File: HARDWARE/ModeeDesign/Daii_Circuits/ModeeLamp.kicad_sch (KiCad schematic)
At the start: 9 parts, among them J4 AC, J5 AC, Q5 2N2222, Q6 IRLZ44N, U5 MOC3023M, U6 ESP32-DEVKIT-V1

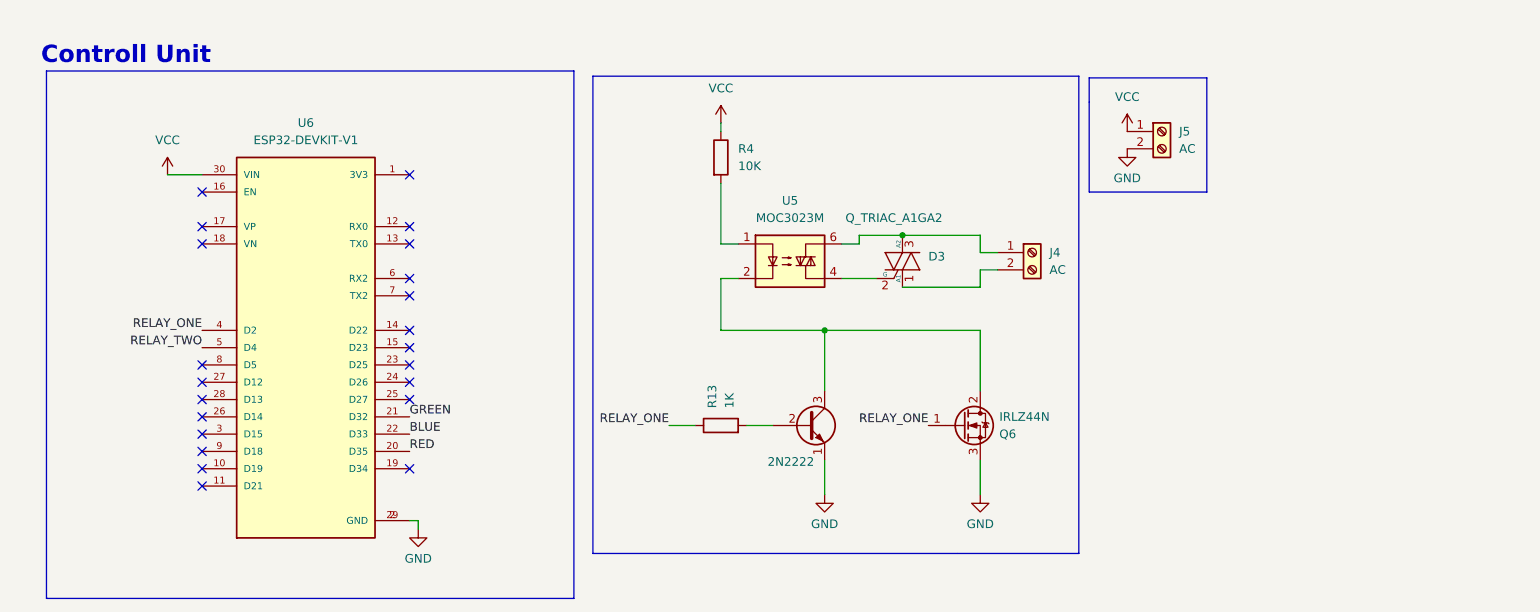
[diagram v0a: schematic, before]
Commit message: WIP: ModeeLamp PCB placement, heater project, Nakheel_Driver updates; ignore .history
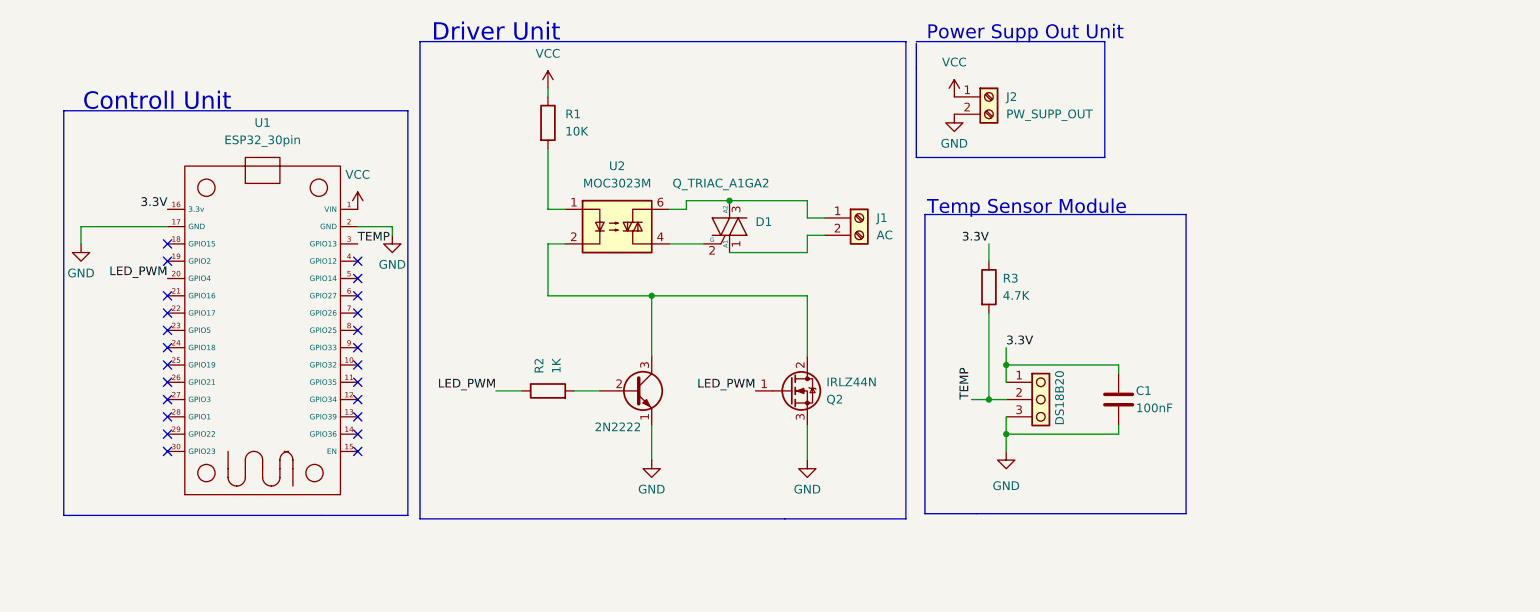
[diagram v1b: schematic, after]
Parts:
- removed U6: ESP32-DEVKIT-V1, RF:MODULE_ESP32_DEVKIT_V1, symbol ESP32-DEVKIT-V1:ESP32-DEVKIT-V1
- added C1: 100nF, Capacitor_THT:C_Disc_D5.0mm_W2.5mm_P2.50mm, symbol Device:C
- added J3: DS18B20, TerminalBlock_Altech:Altech_AK100_1x03_P5.00mm, symbol Connector:Screw_Terminal_01x03
- added R3: 4.7K, Resistor_THT:R_Axial_DIN0204_L3.6mm_D1.6mm_P7.62mm_Horizontal, symbol Device:R
- added U1: (no value), ESP32_30pin, symbol esp32_30pin_revised:ESP32_30Pin
- J1: renamed from J4; footprint TerminalBlock:TerminalBlock_Altech_AK300-2_P5.00mm -> TerminalBlock_Altech:Altech_AK100_1x02_P5.00mm
- J2: renamed from J5; value AC -> PW_SUPP_OUT; footprint TerminalBlock:TerminalBlock_Altech_AK300-2_P5.00mm -> TerminalBlock_Altech:Altech_AK100_1x02_P5.00mm
- renumbered D3 to D1, Q5 to Q1, Q6 to Q2, R4 to R1, R13 to R2, U5 to U2
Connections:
- net GND: now also C1.2, J3.3 (Pin_3), U1.17 (GND), U1.2 (GND)
- net VCC: now also U1.1 (VIN)
- net RELAY_ONE renamed LED_PWM
- net LED_PWM: now also U1.20 (GPIO4)
- new net 3.3V: C1.1, J3.1 (Pin_1), R3.1, U1.16 (3.3v)
- new net TEMP: J3.2 (Pin_2), R3.2, U1.3 (GPIO13)
- no-connect marks 22 -> 24
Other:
- note added: "Driver Unit"
- note added: "Power Supp Out Unit"
- note added: "Temp Sensor Module"
- moved on the sheet: D1, J1, J2, Q2, R1, R2, U2

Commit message: Fixing PCB review points and add interactive BOM
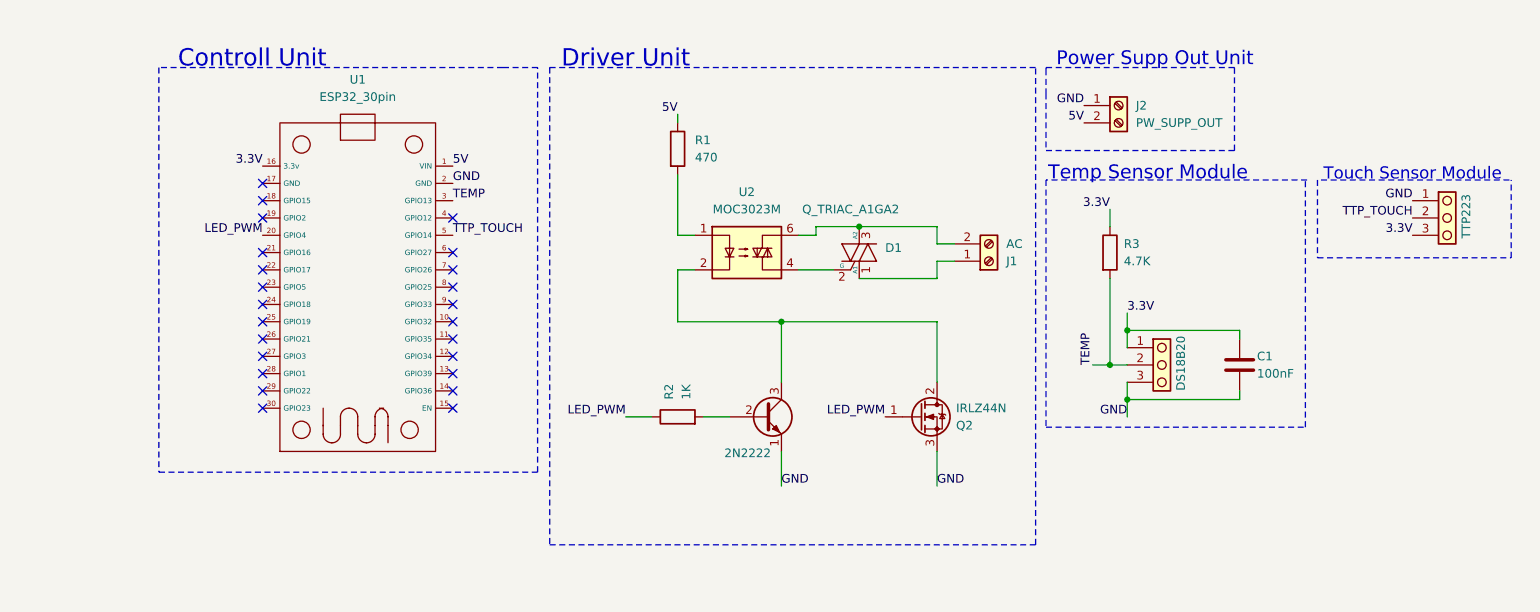
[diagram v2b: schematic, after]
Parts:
- added J4: TTP223, TerminalBlock_Altech:Altech_AK100_1x03_P5.00mm, symbol Connector:Screw_Terminal_01x03
- R1: value 10K -> 470
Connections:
- net 3.3V: now also J4.3 (Pin_3)
- net GND: now also J2.1 (Pin_1), J4.1 (Pin_1); no longer J2.2 (Pin_2), U1.17 (GND)
- net at D1.3 (A2), U2.6: now also J1.2 (Pin_2); no longer J1.1 (Pin_1)
- net at D1.1 (A1): now also J1.1 (Pin_1); no longer J1.2 (Pin_2)
- net TTP_TOUCH: now reaches U1.5 (GPIO14)
- net TTP_TOUCH: now also J4.2 (Pin_2)
- net VCC renamed 5V
- net 5V: now also J2.2 (Pin_2); no longer J2.1 (Pin_1)
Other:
- note added: "Touch Sensor Module"
- moved on the sheet: C1, D1, J1, J2, Q2, R1, R2, R3, U1, U2
